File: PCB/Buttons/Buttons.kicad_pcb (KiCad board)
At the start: 2 copper layers, 78 x 60 mm, 17 parts, among them J1 Conn_02x11_Odd_Even

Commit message: PCB Manufacturing Files and Full CAD
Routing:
- net +5V: track 169.5 -> 178.4 mm, vias 0 -> 1
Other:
- board text added: "Button Panel: ULP12OAP1RSSCL1REDGRN Tolga Cavusoglu September 2025"
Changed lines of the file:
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@@
 		(layer "Edge.Cuts")
+	)
+	(gr_text "Button Panel: ULP12OAP1RSSCL1REDGRN\nTolga Cavusoglu\nSeptember 2025"
+		(at 173.75 112 0)
+		(layer "F.SilkS")
+		(effects
+			(font
+				(size 1 1)
+				(thickness 0.1)
+			)
+			(justify left bottom)
+		)
 	)
 	(segment
@@
 		(start 180.4625 69.5625)
 		(end 178.5 67.6)
-		(width 0.2)
-		(layer "F.Cu")
-		(net 8)
-	)
-	(segment
-		(start 231.5125 74.75)
-		(end 227.74 74.75)
-		(width 0.2)
-		(layer "F.Cu")
-		(net 8)
-	)
-	(segment
-		(start 227.74 74.75)
-		(end 221.99 80.5)
-		(width 0.2)
+		(width 0.5)
+		(layer "F.Cu")
+		(net 8)
+	)
+	(segment
+		(start 232.25 93.75)
+		(end 230.35 93.75)
+		(width 0.5)
+		(layer "F.Cu")
+		(net 8)
+	)
+	(segment
+		(start 200.4 64.5)
+		(end 192.0625 64.5)
+		(width 0.5)
 		(layer "F.Cu")
 		(net 8)
@@
 		(start 212 69.5625)
 		(end 205.4625 69.5625)
-		(width 0.2)
+		(width 0.5)
 		(layer "F.Cu")
 		(net 8)
@@
 		(start 200.1 99)
 		(end 188.4375 99)
-		(width 0.2)
+		(width 0.5)
+		(layer "F.Cu")
+		(net 8)
+	)
+	(segment
+		(start 192.0625 64.5)
+		(end 187 69.5625)
+		(width 0.5)
+		(layer "F.Cu")
+		(net 8)
+	)
+	(segment
+		(start 188.4375 99)
+		(end 187 97.5625)
+		(width 0.5)
+		(layer "F.Cu")
+		(net 8)
+	)
+	(segment
+		(start 180.4625 97.5625)
+		(end 178.5 95.6)
+		(width 0.5)
+		(layer "F.Cu")
+		(net 8)
+	)
+	(segment
+		(start 205.4625 97.5625)
+		(end 203.5 95.6)
+		(width 0.5)
+		(layer "F.Cu")
+		(net 8)
+	)
+	(segment
+		(start 187 97.5625)
+		(end 180.4625 97.5625)
+		(width 0.5)
+		(layer "F.Cu")
+		(net 8)
+	)
+	(segment
+		(start 228.75 67.85)
+		(end 228.5 67.6)
+		(width 0.5)
+		(layer "F.Cu")
+		(net 8)
+	)
+	(segment
+		(start 187 69.5625)
+		(end 180.4625 69.5625)
+		(width 0.5)
 		(layer "F.Cu")
 		(net 8)
@@
 	)
 	(segment
-		(start 191.5625 65)
-		(end 187 69.5625)
-		(width 0.2)
-		(layer "F.Cu")
-		(net 8)
-	)
-	(segment
-		(start 188.4375 99)
-		(end 187 97.5625)
-		(width 0.2)
-		(layer "F.Cu")
-		(net 8)
-	)
-	(segment
-		(start 228.5 67.6)
-		(end 225.9 65)
-		(width 0.2)
-		(layer "F.Cu")
-		(net 8)
-	)
-	(segment
-		(start 180.4625 97.5625)
-		(end 178.5 95.6)
-		(width 0.2)
-		(layer "F.Cu")
-		(net 8)
-	)
-	(segment
-		(start 205.4625 97.5625)
-		(end 203.5 95.6)
-		(width 0.2)
-		(layer "F.Cu")
-		(net 8)
-	)
-	(segment
-		(start 187 97.5625)
-		(end 180.4625 97.5625)
-		(width 0.2)
-		(layer "F.Cu")
-		(net 8)
-	)
-	(segment
-		(start 236.7 69.5625)
-		(end 231.5125 74.75)
-		(width 0.2)
-		(layer "F.Cu")
-		(net 8)
-	)
-	(segment
-		(start 187 69.5625)
-		(end 180.4625 69.5625)
-		(width 0.2)
-		(layer "F.Cu")
-		(net 8)
-	)
-	(segment
 		(start 230.4625 97.5625)
 		(end 228.5 95.6)
@@
 		(start 228.5 95.6)
 		(end 225.1 99)
-		(width 0.2)
+		(width 0.5)
+		(layer "F.Cu")
+		(net 8)
+	)
+	(segment
+		(start 228.5 67.6)
+		(end 225.4 64.5)
+		(width 0.5)
 		(layer "F.Cu")
 		(net 8)
@@
 		(start 203.5 95.6)
 		(end 200.1 99)
-		(width 0.2)
+		(width 0.5)
+		(layer "F.Cu")
+		(net 8)
+	)
+	(segment
+		(start 221.99 80.5)
+		(end 228.75 73.74)
+		(width 0.5)
+		(layer "F.Cu")
+		(net 8)
+	)
+	(segment
+		(start 225.4 64.5)
+		(end 217.25 64.5)
+		(width 0.5)
 		(layer "F.Cu")
 		(net 8)
@@
 	)
 	(segment
-		(start 216.75 65)
-		(end 212.1875 69.5625)
-		(width 0.2)
-		(layer "F.Cu")
-		(net 8)
-	)
-	(segment
-		(start 225.9 65)
-		(end 216.75 65)
-		(width 0.2)
-		(layer "F.Cu")
-		(net 8)
-	)
-	(segment
 		(start 213.4375 99)
 		(end 212 97.5625)
-		(width 0.2)
-		(layer "F.Cu")
-		(net 8)
-	)
-	(segment
-		(start 200.9 65)
-		(end 191.5625 65)
-		(width 0.2)
+		(width 0.5)
+		(layer "F.Cu")
+		(net 8)
+	)
+	(segment
+		(start 228.75 73.74)
+		(end 228.75 67.85)
+		(width 0.5)
 		(layer "F.Cu")
 		(net 8)
@@
 		(start 205.4625 69.5625)
 		(end 203.5 67.6)
-		(width 0.2)
+		(width 0.5)
 		(layer "F.Cu")
 		(net 8)
@@
 	(segment
 		(start 203.5 67.6)
-		(end 200.9 65)
-		(width 0.2)
+		(end 200.4 64.5)
+		(width 0.5)
+		(layer "F.Cu")
+		(net 8)
+	)
+	(segment
+		(start 217.25 64.5)
+		(end 212.1875 69.5625)
+		(width 0.5)
+		(layer "F.Cu")
+		(net 8)
+	)
+	(segment
+		(start 233.5 92.5)
+		(end 232.25 93.75)
+		(width 0.5)
 		(layer "F.Cu")
 		(net 8)
@@
 		(start 212 97.5625)
 		(end 205.4625 97.5625)
-		(width 0.2)
+		(width 0.5)
 		(layer "F.Cu")
 		(net 8)
@@
 		(start 225.1 99)
 		(end 213.4375 99)
-		(width 0.2)
-		(layer "F.Cu")
-		(net 8)
-	)
-	(segment
-		(start 228.5 95.6)
-		(end 220.839 87.939)
-		(width 0.2)
-		(layer "B.Cu")
-		(net 8)
-	)
-	(segment
-		(start 220.839 87.939)
-		(end 220.839 81.651)
-		(width 0.2)
-		(layer "B.Cu")
-		(net 8)
-	)
-	(segment
-		(start 220.839 81.651)
-		(end 221.99 80.5)
-		(width 0.2)
-		(layer "B.Cu")
-		(net 8)
+		(width 0.5)
+		(layer "F.Cu")
+		(net 8)
+	)
+	(segment
+		(start 230.35 93.75)
+		(end 228.5 95.6)
+		(width 0.5)
+		(layer "F.Cu")
+		(net 8)
+	)
+	(via
+		(at 233.5 92.5)
+		(size 0.6)
+		(drill 0.3)
+		(layers "F.Cu" "B.Cu")
+		(net 8)
+	)
+	(segment
+		(start 227 78.25)
+		(end 234.75 86)
+		(width 0.5)
+		(layer "B.Cu")
+		(net 8)
+	)
+	(segment
+		(start 234.75 86)
+		(end 234.75 91.25)
+		(width 0.5)
+		(layer "B.Cu")
+		(net 8)
+	)
+	(segment
+		(start 234.75 91.25)
+		(end 233.5 92.5)
+		(width 0.5)
+		(layer "B.Cu")
+		(net 8)
+	)
+	(segment
+		(start 224.24 78.25)
+		(end 227 78.25)
+		(width 0.5)
+		(layer "B.Cu")
+		(net 8)
+	)
+	(segment
+		(start 221.99 80.5)
+		(end 224.24 78.25)
+		(width 0.5)
+		(layer "B.Cu")
+		(net 8)

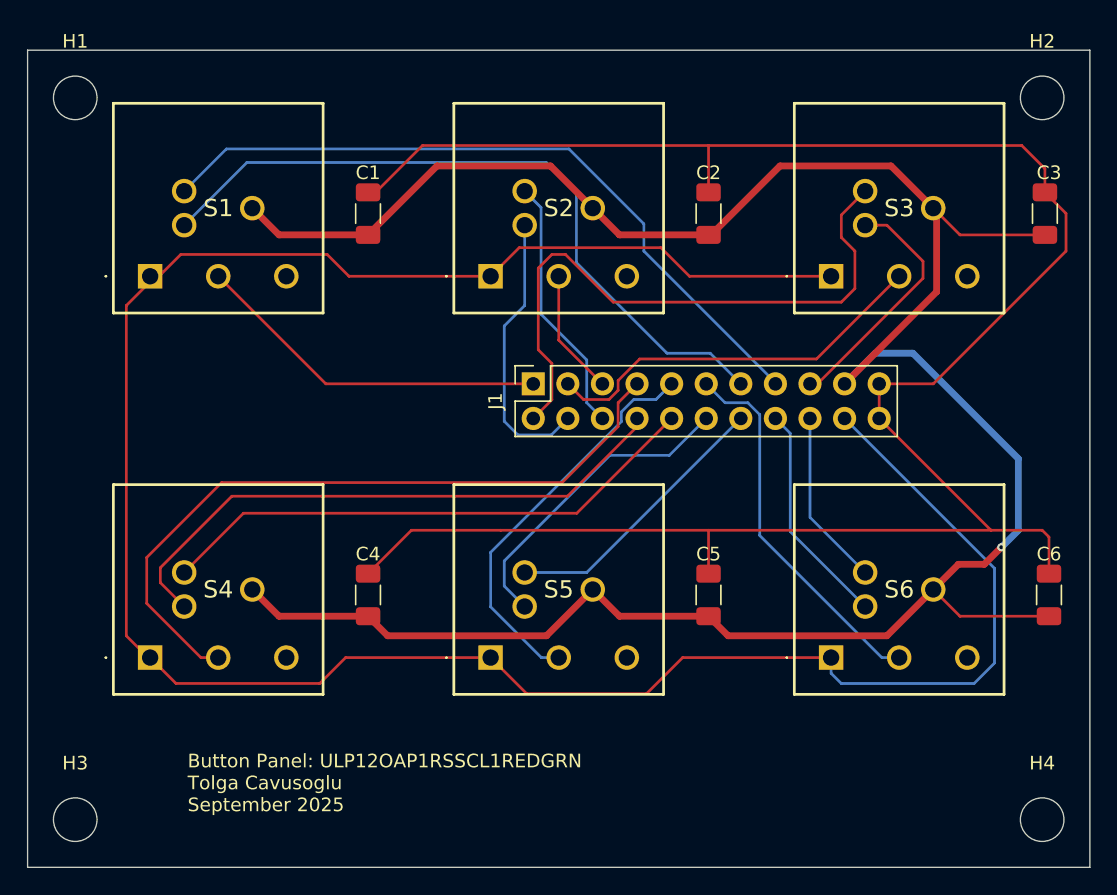
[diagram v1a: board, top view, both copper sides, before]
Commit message: Update main and button pcbs to fix errors with v1.0
Added pull downs to gpio expander and changed header footprint
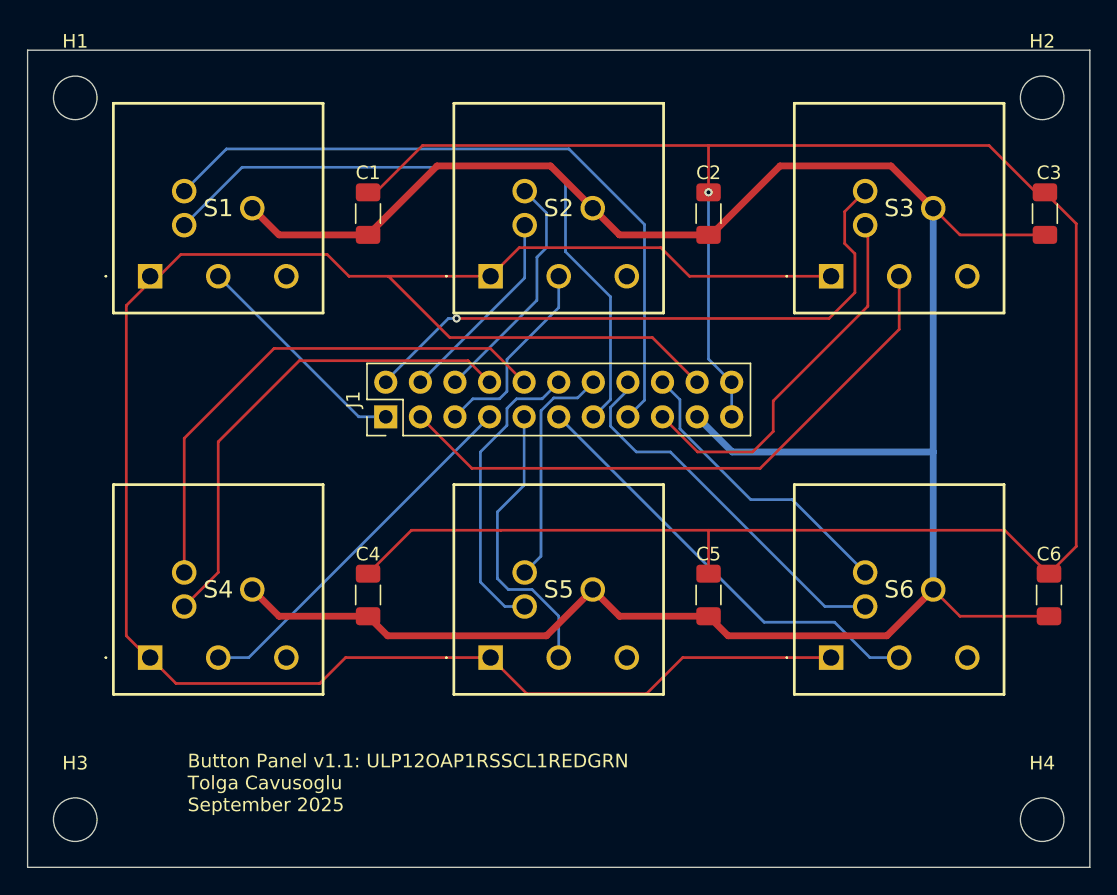
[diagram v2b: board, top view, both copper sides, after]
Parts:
- J1: footprint Connector_PinSocket_2.54mm:PinSocket_2x11_P2.54mm_Vertical -> Connector_PinHeader_2.54mm:PinHeader_2x11_P2.54mm_Vertical
- moved J1 11.1 mm to (188.3, 82.9)
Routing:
- net /Buttons3: track 52.6 -> 27.2 mm
- net /Buttons1: track 29.0 -> 44.9 mm
- net /LED10: track 16.5 -> 27.9 mm
- net +3.3V: track 173.4 -> 162.7 mm
- net /LED2: track 18.1 -> 28.4 mm
- net /Buttons0: track 26.4 -> 16.6 mm
- net /LED11: track 13.0 -> 21.9 mm
- net /Buttons4: track 29.4 -> 21.4 mm
- net /LED6: track 43.5 -> 36.2 mm
- net GND: track 151.3 -> 158.5 mm, vias 0 -> 1
- net /LED4: track 20.6 -> 14.7 mm
- net /Buttons2: track 9.23 -> 14.6 mm
- net /Buttons5: track 27.7 -> 32.3 mm
- net /LED9: track 20.6 -> 17.1 mm
- net /LED0: track 52.5 -> 49.4 mm
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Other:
- board text added: "Button Panel v1.1: ULP12OAP1RSSCL1REDGRN Tolga Cavusoglu September 2025"
- board text removed: "Button Panel: ULP12OAP1RSSCL1REDGRN Tolga Cavusoglu September 2025"
